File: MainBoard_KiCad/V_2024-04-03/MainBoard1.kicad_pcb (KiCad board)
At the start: 2 copper layers, 111.8 x 119 mm, 32 parts, among them J1 BAR02 Pressure Sensor, J3 Conn_01x10_Pin, J4 TSW-103-08-G-T-RA, U2 Pi_Pico_1, U3 AMS1117-3.3, U4 Water Leak Sensor, U5 Orange_Pi5+, U6 Temperature Sensor, U7 SHT30, U8 IMU

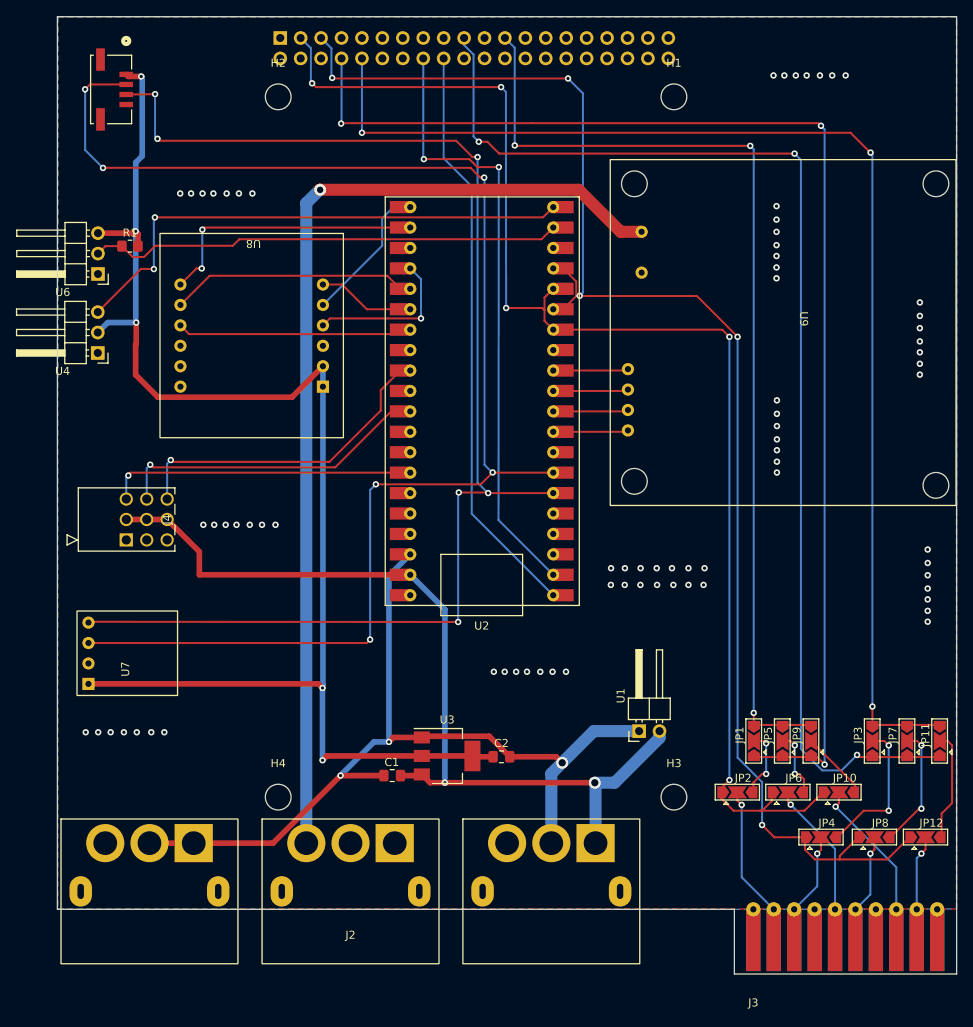
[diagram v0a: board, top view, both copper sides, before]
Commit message: Fixed DRC errors
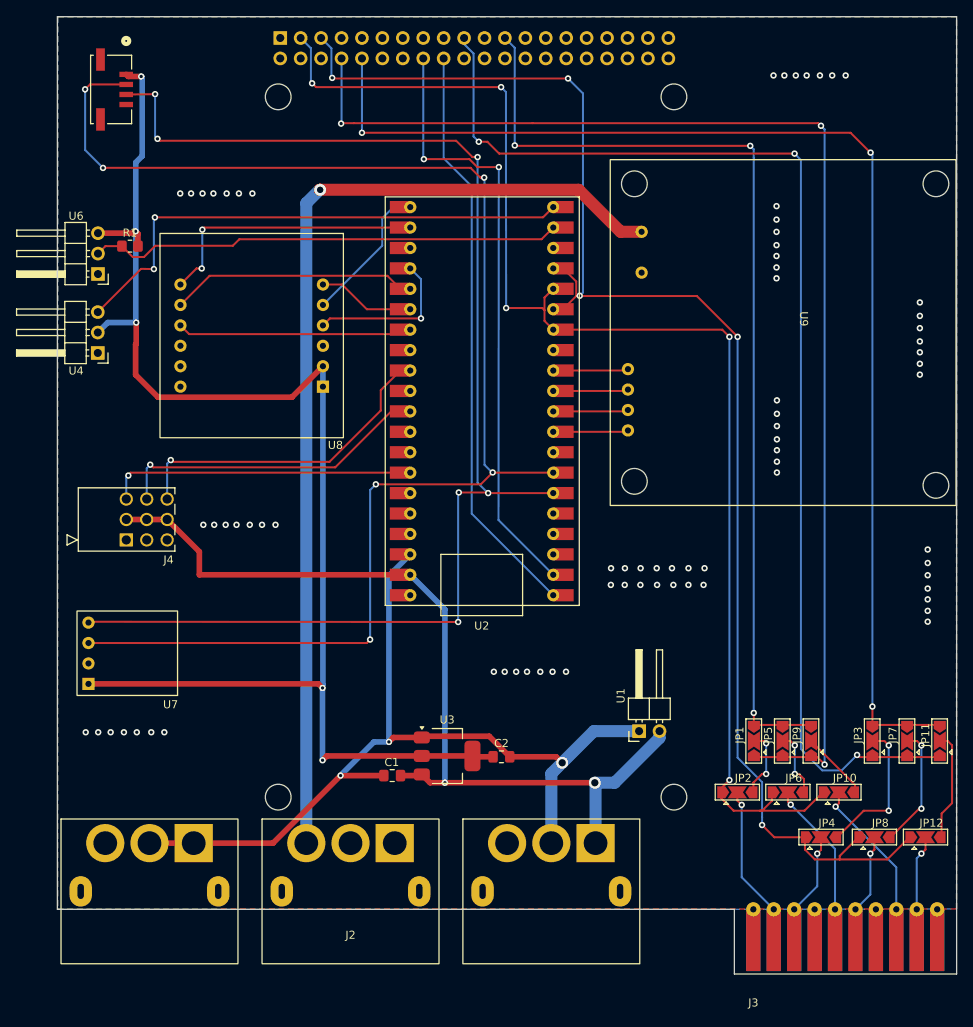
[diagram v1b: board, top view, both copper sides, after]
